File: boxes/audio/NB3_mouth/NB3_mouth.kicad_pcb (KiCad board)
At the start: 2 copper layers, 20 x 18 mm, 8 parts, among them IC1 MAX98357AETE+T, J1 Conn_02x03_Odd_Even, J2 Conn_02x03_Odd_Even, J3 Conn_01x02

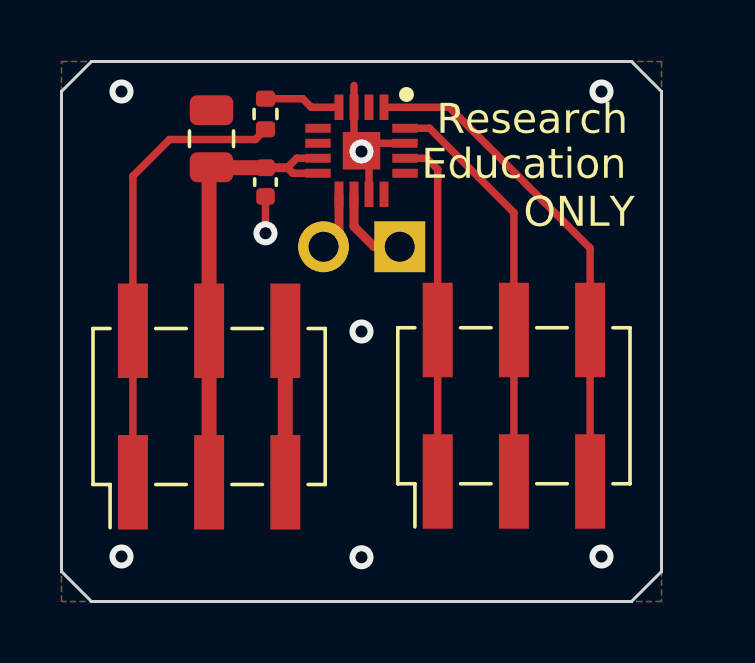
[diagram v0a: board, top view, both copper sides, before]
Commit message: Update NB3 mouth for better panelization (rev 3)
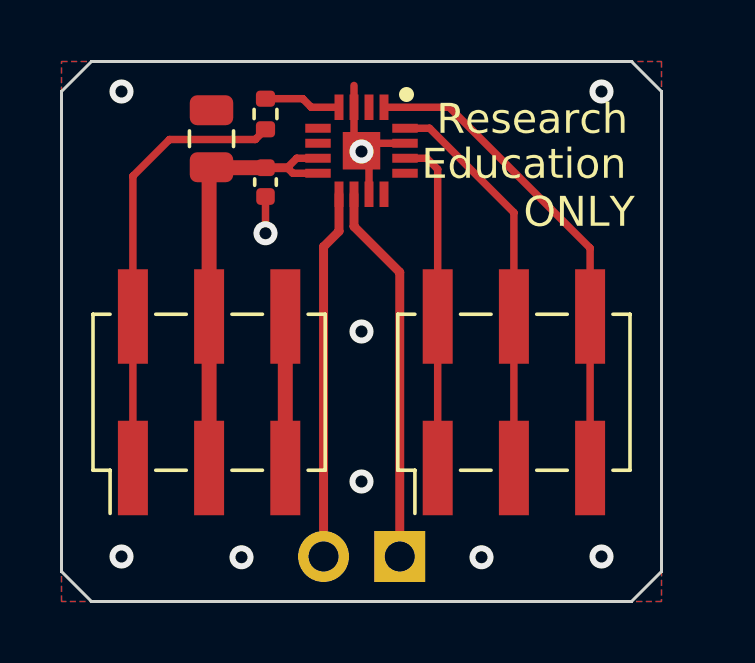
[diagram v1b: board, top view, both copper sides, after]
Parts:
- moved J3 10.3 mm to (152.7, 114.5)
- moved J1 0.47 mm to (146.3, 109.0)
- moved J2 0.45 mm to (156.5, 109.0)
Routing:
- net /Speaker+: track 1.96 -> 12.3 mm
- net /Speaker-: track 2.88 -> 12.7 mm
- net GND: vias 8 -> 10
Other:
- board text added: "-+"
- board text added: "NB3 Rev Mouth 0.0.3"
- board text removed: "NB3 Mouth Rev 0.0.2"
